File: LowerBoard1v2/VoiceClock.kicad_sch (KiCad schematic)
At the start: 39 parts, among them U1001 74HC74, U1002 74HC595, U1003 74HC74, U1004 74HC08, U1005 74HC595, U1006 74HC14, U1007 74HC14

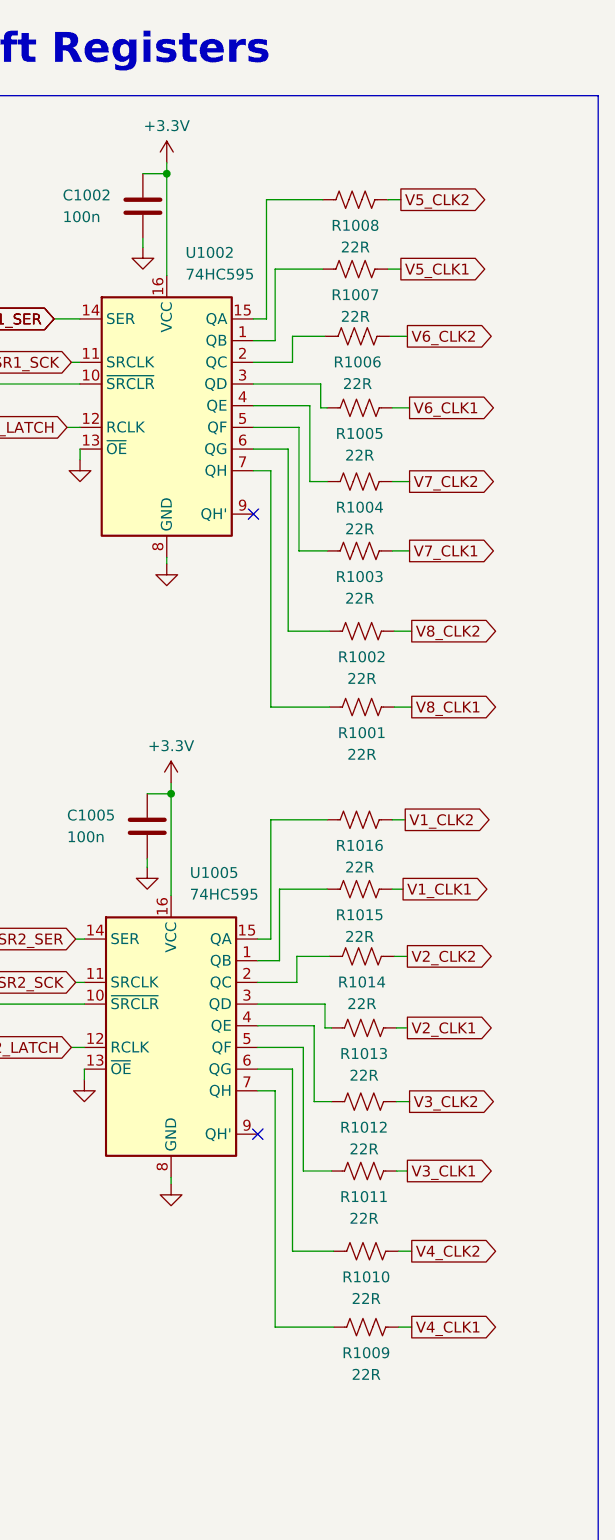
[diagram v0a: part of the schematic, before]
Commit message: switched to resistor arrays for schematic
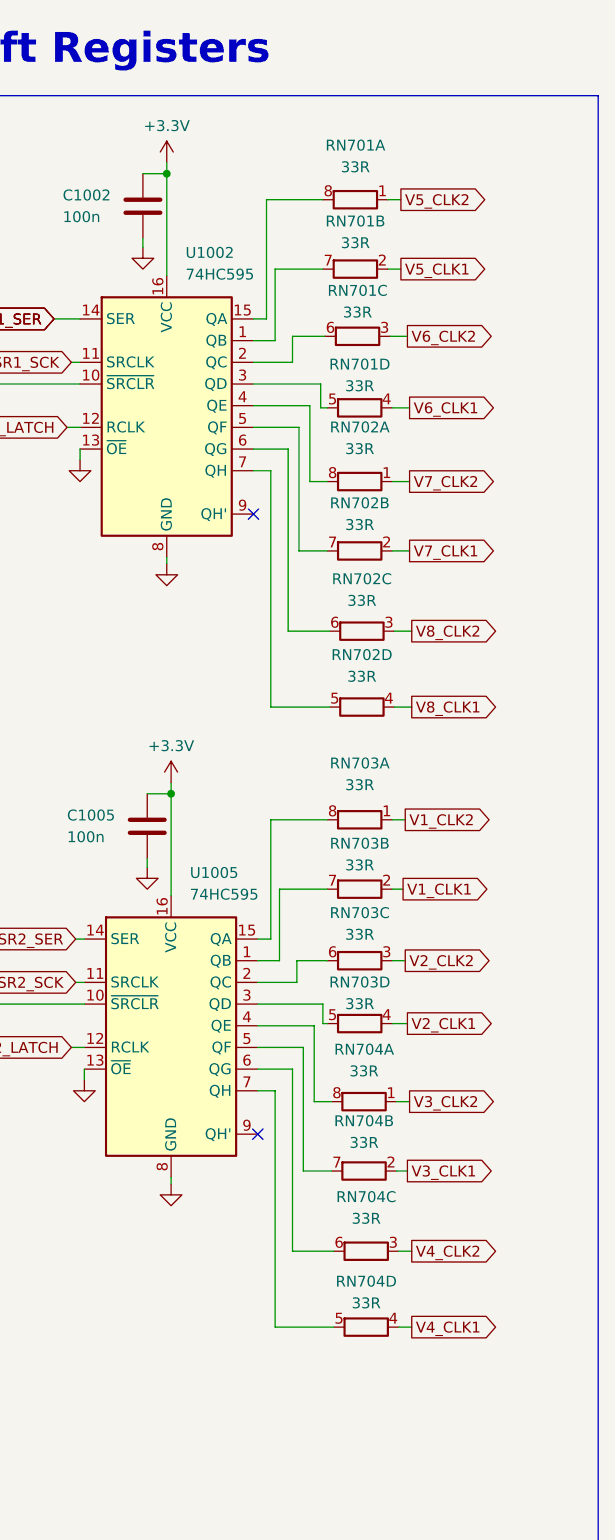
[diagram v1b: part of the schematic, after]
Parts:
- removed R1001, R1002, R1003, R1004, R1005, R1006, R1007, R1008, R1009, R1010, R1011, R1012, R1013, R1014, R1015, R1016: 22R, Resistor_SMD:R_0805_2012Metric, symbol Device:R_US
- added RN701, RN702, RN703, RN704: 33R, Resistor_SMD:R_Array_Concave_4x0603, symbol Device:R_Pack04_Split
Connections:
- net V1_CLK1: now also RN703.2 (R2.1)
- net V1_CLK2: now also RN703.1 (R1.1)
- net V2_CLK1: now also RN703.4 (R4.1)
- net V2_CLK2: now also RN703.3 (R3.1)
- net V3_CLK1: now also RN704.2 (R2.1)
- net V3_CLK2: now also RN704.1 (R1.1)
- net V4_CLK1: now also RN704.4 (R4.1)
- net V4_CLK2: now also RN704.3 (R3.1)
- net V5_CLK1: now also RN701.2 (R2.1)
- net V5_CLK2: now also RN701.1 (R1.1)
- net V6_CLK1: now also RN701.4 (R4.1)
- net V6_CLK2: now also RN701.3 (R3.1)
- net V7_CLK1: now also RN702.2 (R2.1)
- net V7_CLK2: now also RN702.1 (R1.1)
- net V8_CLK1: now also RN702.4 (R4.1)
- net V8_CLK2: now also RN702.3 (R3.1)
- net at U1005.7 (QH): now also RN704.5 (R4.2)
- net at U1005.4 (QE): now also RN704.8 (R1.2)
- net at U1002.4 (QE): now also RN702.8 (R1.2)
- net at U1002.15 (QA): now also RN701.8 (R1.2)
- net at U1002.1 (QB): now also RN701.7 (R2.2)
- net at U1002.5 (QF): now also RN702.7 (R2.2)
- net at U1005.1 (QB): now also RN703.7 (R2.2)
- net at U1005.15 (QA): now also RN703.8 (R1.2)
- net at U1005.2 (QC): now also RN703.6 (R3.2)
- net at U1005.3 (QD): now also RN703.5 (R4.2)
- net at U1005.5 (QF): now also RN704.7 (R2.2)
- net at U1005.6 (QG): now also RN704.6 (R3.2)
- net at U1002.3 (QD): now also RN701.5 (R4.2)
- net at U1002.2 (QC): now also RN701.6 (R3.2)
- net at U1002.7 (QH): now also RN702.5 (R4.2)
- net at U1002.6 (QG): now also RN702.6 (R3.2)

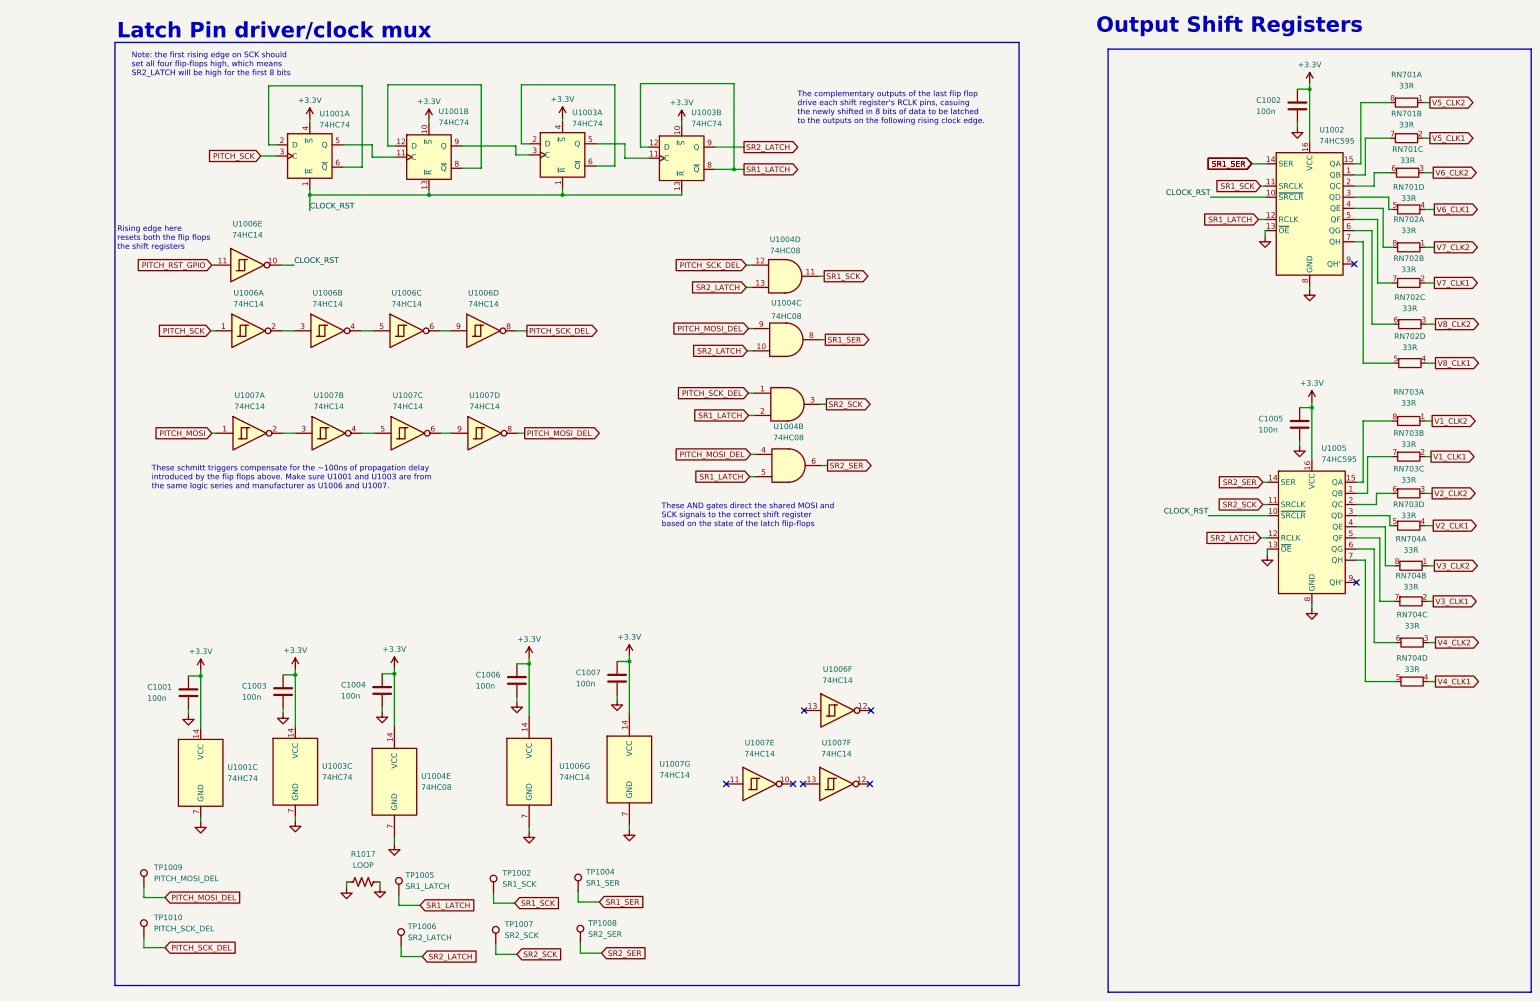
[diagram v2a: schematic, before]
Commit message: simplified voice clock a bit
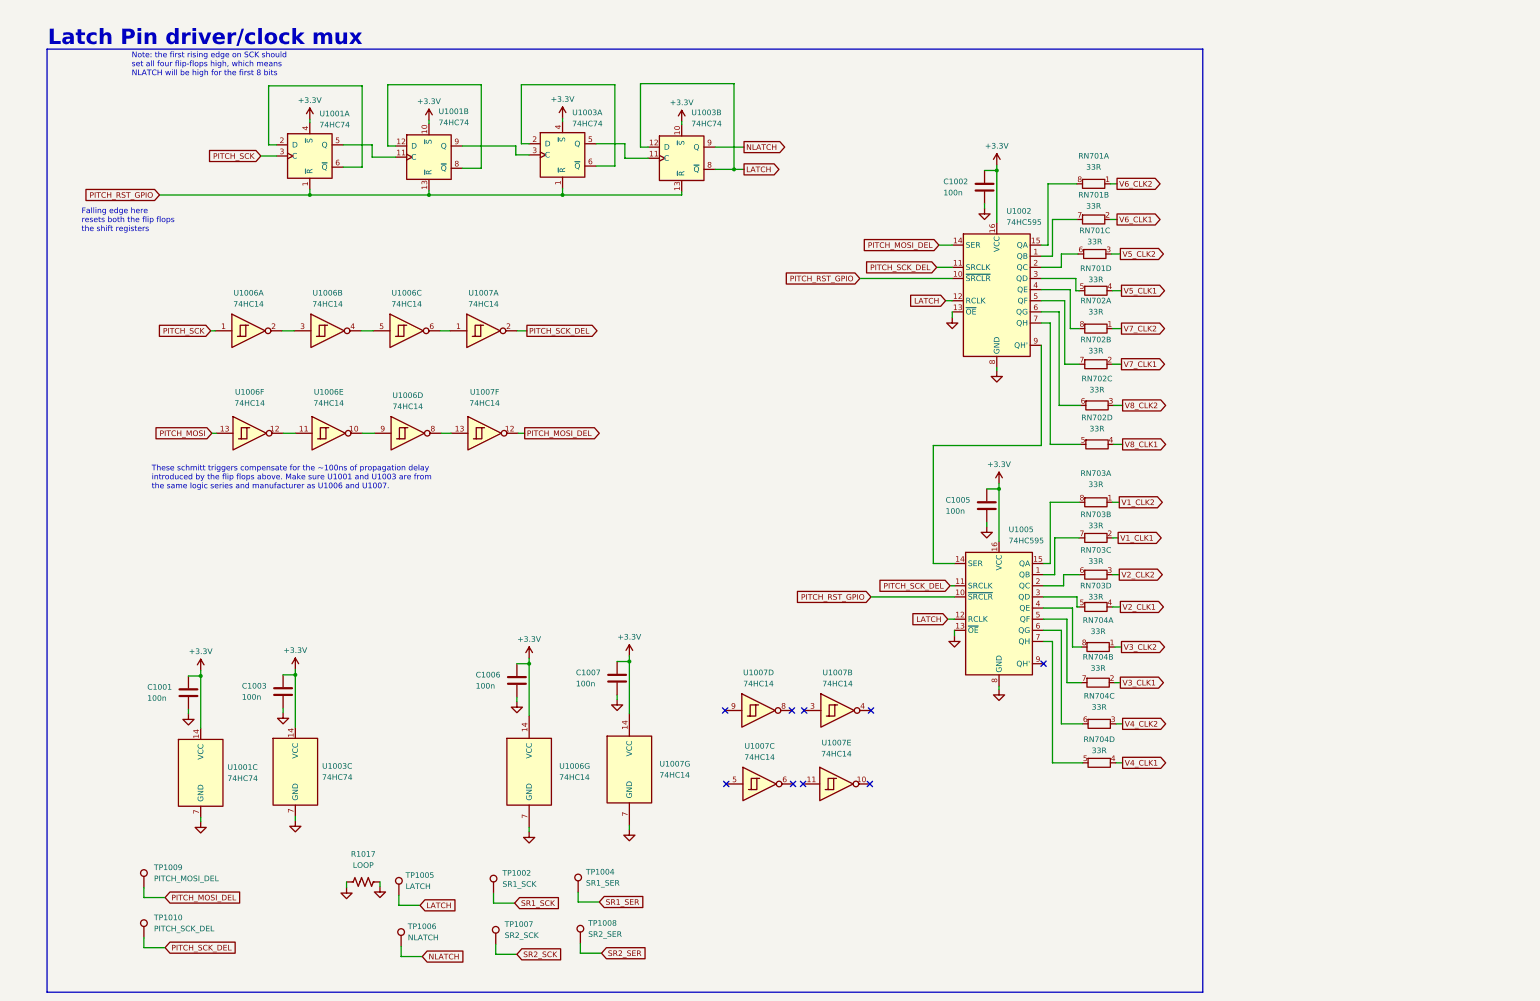
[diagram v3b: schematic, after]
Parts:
- removed C1004: 100n, Capacitor_SMD:C_0805_2012Metric, symbol Device:C
- removed U1004: 74HC08, Package_SO:SOIC-14_3.9x8.7mm_P1.27mm, symbol 74xx:74LS08
- TP1005: value SR1_LATCH -> LATCH
- TP1006: value SR2_LATCH -> NLATCH
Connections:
- net PITCH_MOSI: now also U1006.13; no longer U1007.1
- net PITCH_MOSI_DEL: now also U1002.14 (SER), U1007.12; no longer U1007.8
- net PITCH_RST_GPIO: now also U1001.1 (~{R}), U1001.13 (~{R}), U1002.10 (~{SRCLR}), U1003.1 (~{R}), U1003.13 (~{R}), U1005.10 (~{SRCLR}); no longer U1006.11
- net PITCH_SCK_DEL: now also U1002.11 (SRCLK), U1005.11 (SRCLK), U1007.2; no longer U1006.8
- net SR1_SCK: no longer U1002.11 (SRCLK)
- net SR1_SER: no longer U1002.14 (SER)
- net SR2_SCK: no longer U1005.11 (SRCLK)
- net SR2_SER: no longer U1005.14 (SER)
- net V5_CLK1: now also RN701.4 (R4.1); no longer RN701.2 (R2.1)
- net V5_CLK2: now also RN701.3 (R3.1); no longer RN701.1 (R1.1)
- net V6_CLK1: now also RN701.2 (R2.1); no longer RN701.4 (R4.1)
- net V6_CLK2: now also RN701.1 (R1.1); no longer RN701.3 (R3.1)
- net at U1006.12: now also U1006.11
- net at U1007.3: no longer U1007.2
- net at U1007.4: no longer U1007.5
- net at U1007.6: no longer U1007.9
- net at U1006.6: now also U1007.1; no longer U1006.9
- net at U1007.13: now also U1006.8
- net at U1002.9 (QH'): now also U1005.14 (SER)
- removed net CLOCK_RST: U1001.1 (~{R}), U1001.13 (~{R}), U1002.10 (~{SRCLR}), U1003.1 (~{R}), U1003.13 (~{R}), U1005.10 (~{SRCLR}), U1006.10
- net SR1_LATCH renamed LATCH
- net LATCH: now also U1005.12 (RCLK)
- net SR2_LATCH renamed NLATCH
- net NLATCH: no longer U1005.12 (RCLK)
- new net: U1006.10, U1006.9
- no-connect marks 8 -> 9
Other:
- note added: "Falling edge here resets both the flip flops the shift registers"
- note added: "Note: the first rising edge on SCK should set all four flip-flops high, which means NLATCH will be high for the first 8 bits"
- note removed: "Note: the first rising edge on SCK should set all four flip-flops high, which means SR2_LATCH will be high for the first 8 bits"
- note removed: "Output Shift Registers"
- note removed: "Rising edge here resets both the flip flops the shift registers"
- note removed: "The complementary outputs of the last flip flop drive each shift register's RCLK pins, casuing the newly shifted in 8 bits of data to be latched to the outputs on the following rising clock edge."
- note removed: "These AND gates direct the shared MOSI and SCK signals to the correct shift register based on the state of the latch flip-flops"
- moved on the sheet: C1002, C1005, RN701A, RN701B, RN701C, RN701D, RN702A, RN702B, RN702C, RN702D, RN703A, RN703B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
